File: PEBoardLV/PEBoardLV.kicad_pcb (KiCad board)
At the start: 2 copper layers, 113.7 x 78.7 mm, 69 parts, among them J1 BSPD Test Jumper, J10 ECU Debug Connector, J11 SWD Header, J12 Extra Pin Header, J13 CAN Header, J14 UART Header, J15 To TSAL, J2 Beam Interlock, J3 To HV Interlocks, J4 To Left Panel, J5 To Right Panel, J6 To Brake Light, J7 To PE HV, J8 BSPD Reset, J9 Main LV Connector, U1 MCP6004, U10 ISO1050, U11 STM32F405, U2 4072, U3 4071, U4 DE1A1B-L2-12V, U5 74HC595, U6 LM555N, U7 SN754410, U8 NCP1117DT33RKG, U9 L78S05CV-DG, Y1 8MHz

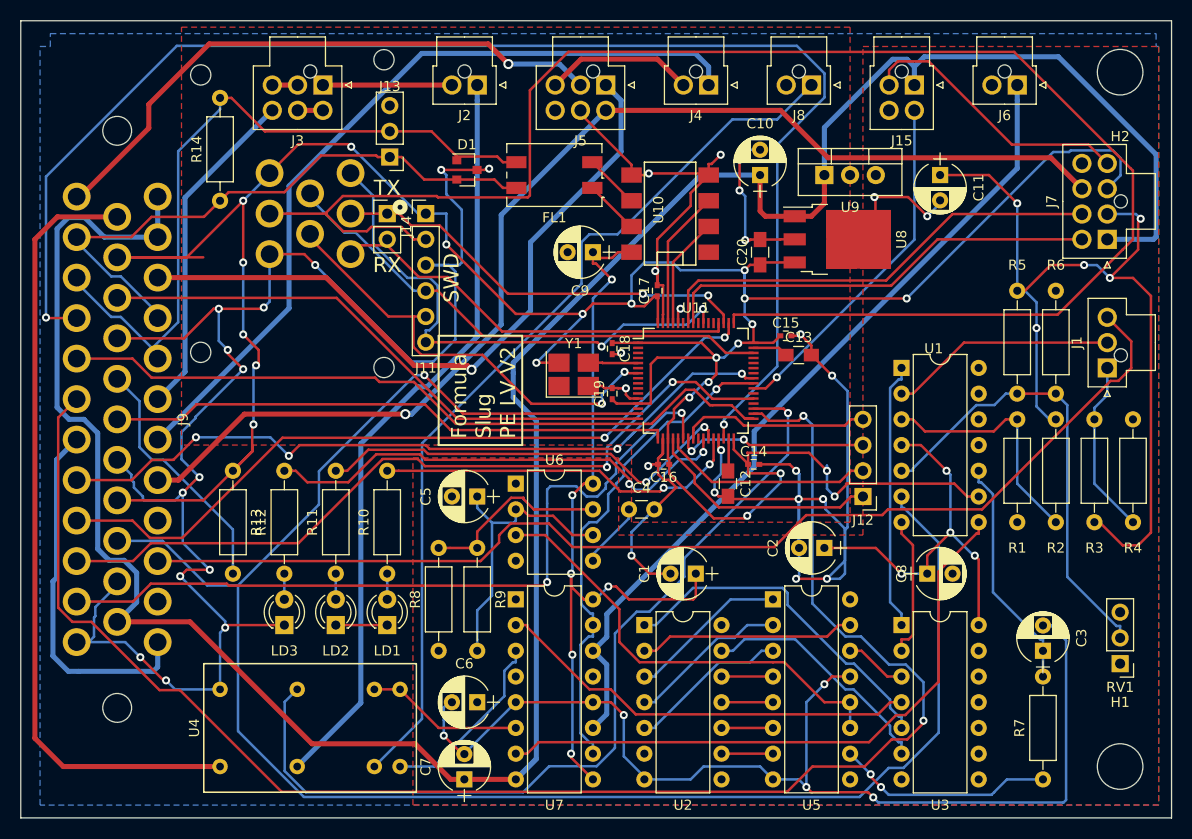
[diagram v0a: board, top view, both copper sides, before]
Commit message: Add more ground/vcc plane bridges to PE LV pcb
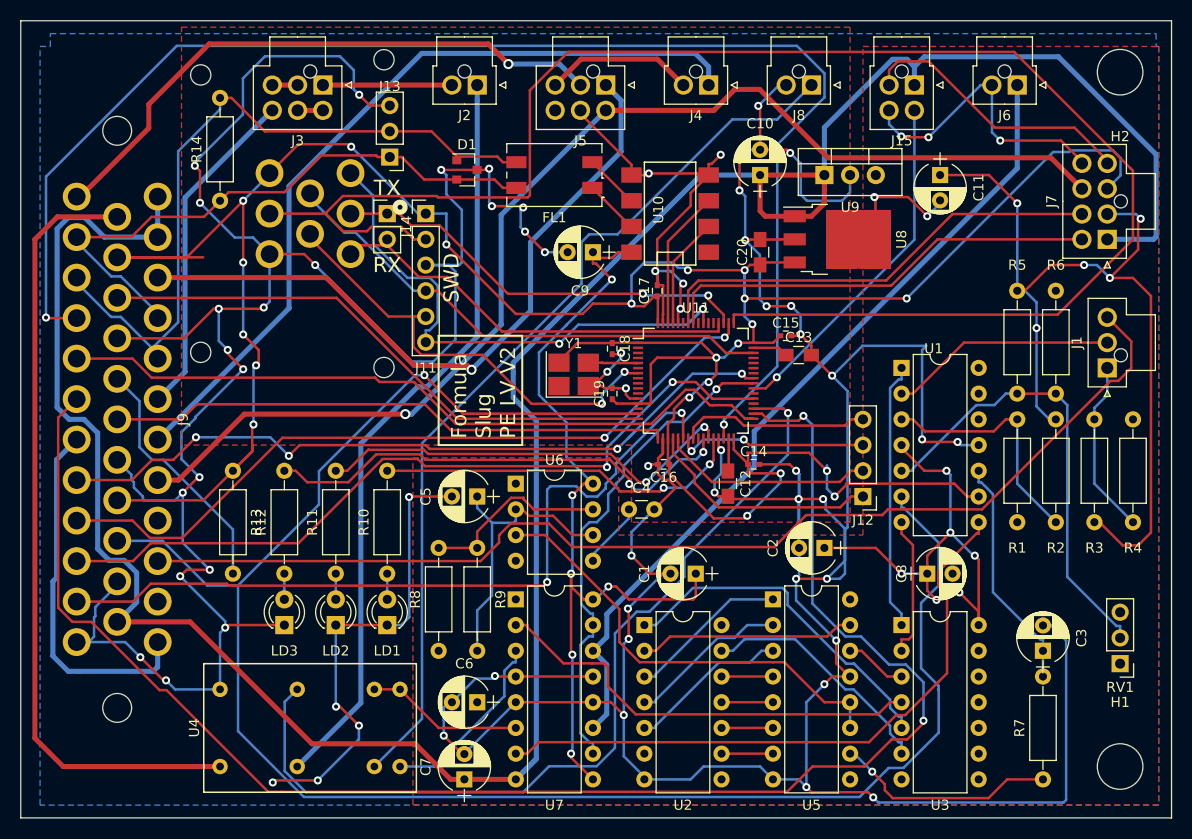
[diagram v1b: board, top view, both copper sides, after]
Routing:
- net GND: track 460.5 -> 703.4 mm, vias 41 -> 68
- net +5V: track 226.0 -> 240.6 mm, vias 17 -> 18
- net +12V: track 256.8 -> 263.1 mm
- net +3V3: track 307.8 -> 305.0 mm, vias 22 -> 21
- net /SWO: track 52.8 -> 54.7 mm
- net /AIRS_FINAL: track 116.0 -> 117.7 mm
- net /SIG_BSE: track 179.3 -> 180.7 mm
- net /BSPD_FLT: track 42.4 -> 43.5 mm
- net /TIMER: track 62.2 -> 62.9 mm

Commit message: Select 4 layer version of PE LV board
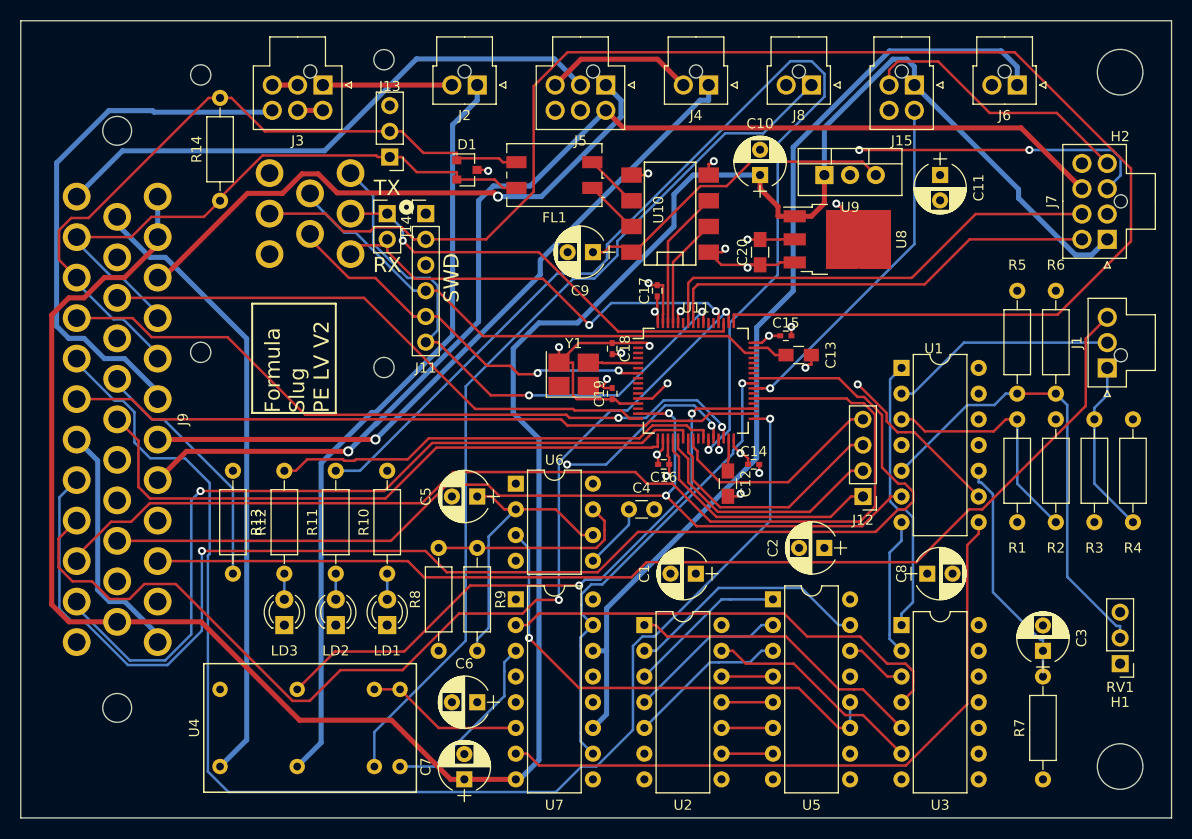
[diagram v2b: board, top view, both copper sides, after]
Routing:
- net GND: track 703.4 -> 50.7 mm, vias 68 -> 16
- net +3V3: track 305.0 -> 108.5 mm, vias 21 -> 11
- net +5V: track 240.6 -> 51.2 mm, vias 18 -> 0
- net /BUTTON_3: track 159.7 -> 68.4 mm, vias 2 -> 0
- net /SIG_BSE: track 180.7 -> 94.6 mm, vias 1 -> 2
- net /BUTTON_1: track 140.5 -> 70.9 mm
- net /STATUS_LED_2: track 42.2 -> 109.5 mm, vias 2 -> 1
- net /LED_AMS: track 74.4 -> 137.5 mm, vias 4 -> 1
- net /BUTTON_2: track 72.9 -> 132.9 mm, vias 0 -> 1
- net /LED_BSPD: track 76.7 -> 107.2 mm, vias 2 -> 0
- net /LED_IMD: track 74.5 -> 103.1 mm
- net /BSPD_FLT_LATCHED: track 88.4 -> 60.9 mm, vias 1 -> 2
- net +12V: track 263.1 -> 236.1 mm
- net /AIRS_PEINTERLOCKS_OUT: track 33.2 -> 53.1 mm
- net /AIRS_BOTS_OUT: track 77.8 -> 61.6 mm
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- added copper zone on In1.Cu, net +3V3
- added copper zone on In1.Cu, net +5V
- added copper zone on In2.Cu, net GND
- removed copper zone on F.Cu, net +3V3
- removed copper zone on F.Cu, net +5V
- removed copper zone on B.Cu, net GND
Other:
- copper layers 2 -> 4

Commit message: Revise boards based on design review
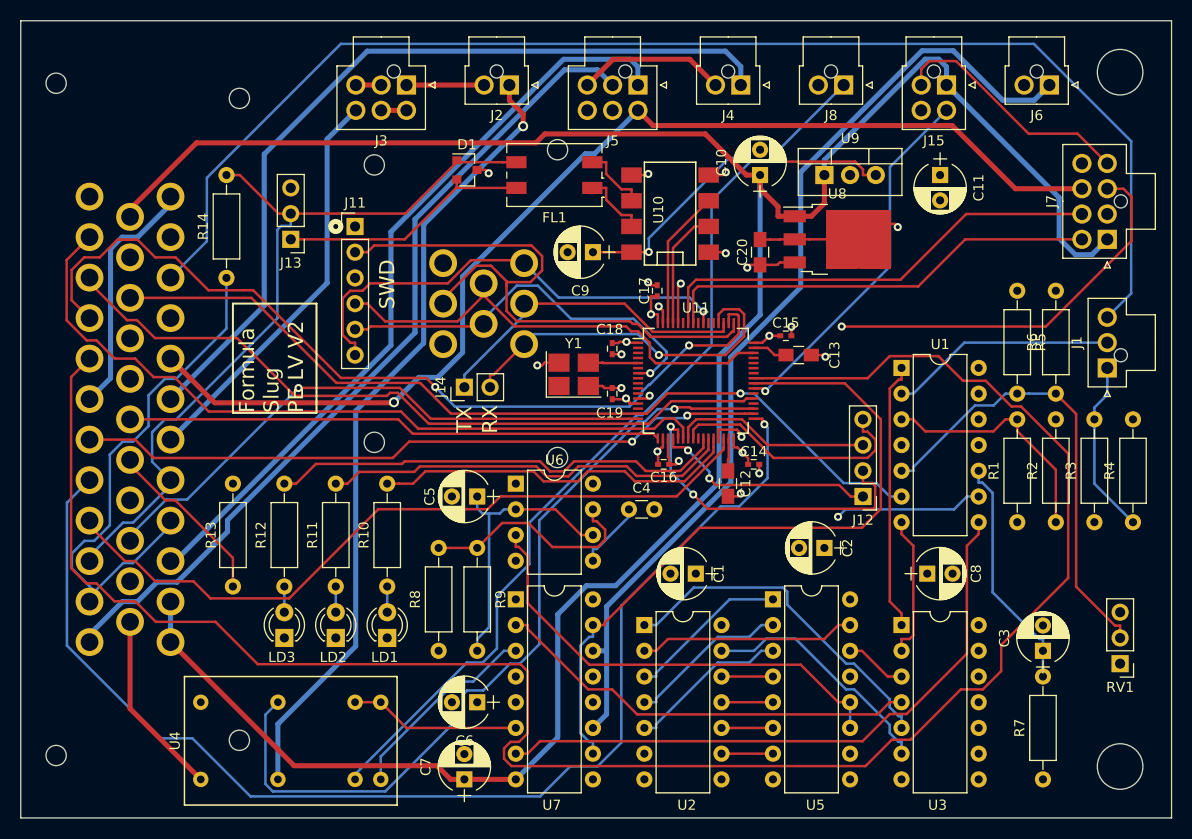
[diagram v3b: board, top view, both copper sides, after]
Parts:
- J9: footprint FSFootprints:Ampseal - 35 pin -> FSFootprints:Ampseal-776231; moved to B.Cu
- moved J10 19.3 mm to (97.2, 57.1)
- moved J14 18.8 mm to (95.2, 65.4), turned to 90 degrees
- moved J13 12.7 mm to (78.1, 50.8)
- moved J3 8.25 mm to (89.5, 35.6)
- moved R14 7.65 mm to (71.8, 54.6)
- moved J11 7.10 mm to (84.5, 49.5)
- moved J15 3.18 mm to (142.9, 35.6)
- moved J4 3.18 mm to (122.6, 35.6)
- moved J8 3.18 mm to (132.7, 35.6)
- moved J2 3.17 mm to (99.7, 35.6)
- moved J5 3.17 mm to (112.4, 35.6)
- moved J6 3.17 mm to (153.0, 35.6)
- moved U4 2.29 mm to (76.8, 96.5)
- moved R10 1.27 mm to (87.6, 85.1)
- moved R11 1.27 mm to (82.5, 85.1)
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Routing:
- net /SWCLK: track 155.2 -> 60.8 mm
- net /STATUS_LED_2: track 109.5 -> 40.9 mm, vias 1 -> 0
- net /LED_AMS: track 137.5 -> 194.4 mm, vias 1 -> 0
- net /AIRS_BOTS_OUT: track 61.6 -> 18.5 mm
- net /LED_BSPD: track 107.2 -> 73.1 mm
- net /12V_LVMS: track 56.5 -> 83.4 mm
- net +3V3: track 108.5 -> 82.3 mm
- net /CAN_H: track 60.6 -> 85.0 mm
- net /SIG_BRAKELT: track 46.4 -> 70.4 mm, vias 1 -> 0
- net /SIG_CURRENT: track 109.0 -> 130.5 mm
- net /BSPD_FLT_LATCHED: track 60.9 -> 81.1 mm, vias 2 -> 1
- net +5V: track 51.2 -> 33.6 mm, vias 0 -> 2
- net /12V_SRC: track 58.0 -> 75.4 mm, vias 1 -> 0
- net /LED_IMD: track 103.1 -> 86.3 mm
- net /AIRS_PEINTERLOCKS_OUT: track 53.1 -> 40.1 mm
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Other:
- net class 3.3V: clearance 0.205 -> 0.24
- net class Default: clearance 0.205 -> 0.24
- net class Ground: clearance 0.205 -> 0.24
- net class HighSpeed: clearance 0.205 -> 0.24
- rule trace_clearance: 0.205 -> 0.24

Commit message: Add connections to connectors on PE and Acc LV boards
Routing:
- net +5V: track 33.6 -> 54.6 mm
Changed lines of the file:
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@@
   (general
     (links 232)
-    (no_connects 1)
+    (no_connects 0)
     (area 45.804999 27.715 165.150001 109.545)
     (thickness 1.6)
     (drawings 13)
-    (tracks 940)
+    (tracks 946)
     (zones 0)
     (modules 69)
@@
   (layers
     (0 F.Cu signal)
-    (1 In1.Cu power hide)
-    (2 In2.Cu power hide)
+    (1 In1.Cu power)
+    (2 In2.Cu power)
     (31 B.Cu signal)
     (32 B.Adhes user)
@@
     (effects (font (size 1.5 1.5) (thickness 0.3)))
   )
+  (segment (start 158.75 48.3) (end 159.552 48.3) (width 0.25) (layer In1.Cu) (net 1) (status C00000))
+  (segment (start 159.552 48.3) (end 161.925 50.673) (width 0.25) (layer In1.Cu) (net 1) (status 400000))
+  (segment (start 161.925 50.673) (end 161.925 54.102) (width 0.25) (layer In1.Cu) (net 1))
+  (segment (start 161.925 54.102) (end 161.163 53.34) (width 0.25) (layer In1.Cu) (net 1))
+  (segment (start 161.163 53.34) (end 152.4 53.34) (width 0.25) (layer In1.Cu) (net 1))
+  (segment (start 152.4 53.34) (end 149.86 55.88) (width 0.25) (layer In1.Cu) (net 1) (status 800000))
   (via (at 122.7642 42.7522) (size 0.8) (layers F.Cu B.Cu) (net 1))
   (via (at 113.4667 52.05) (size 0.8) (layers F.Cu B.Cu) (net 1))

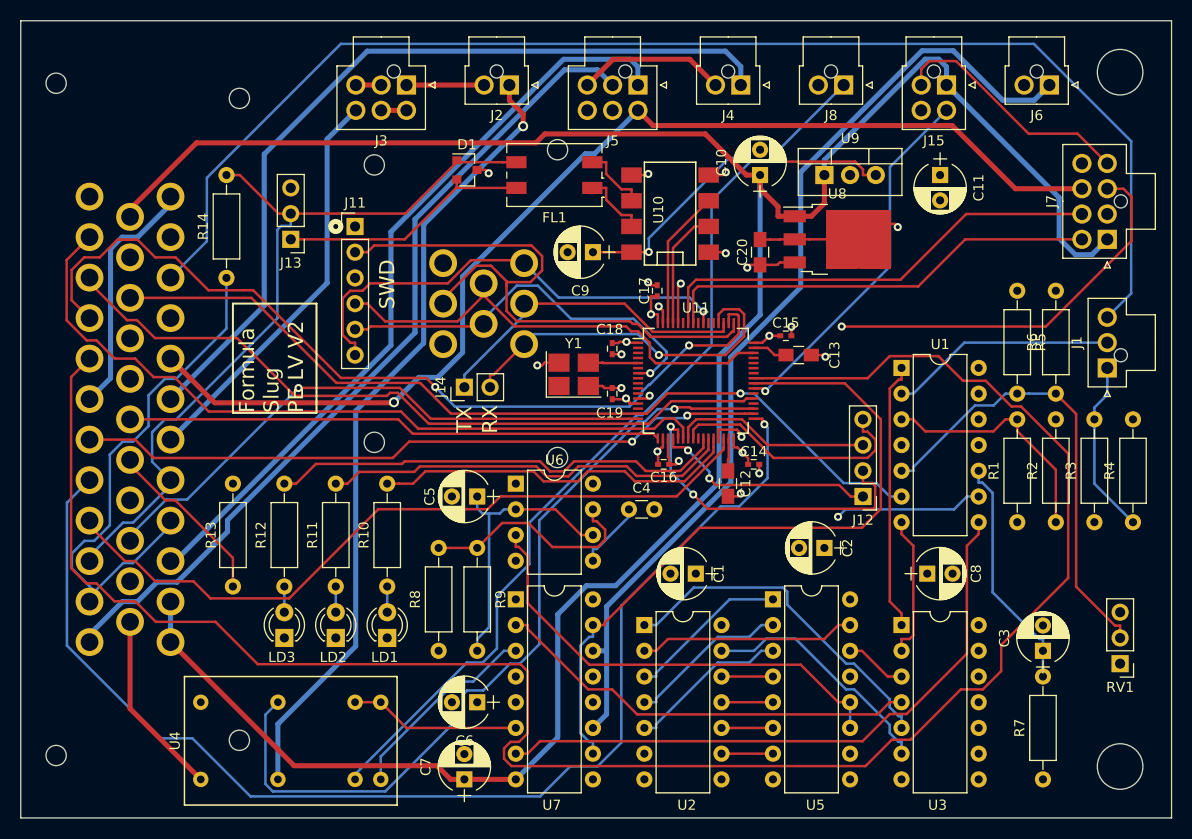
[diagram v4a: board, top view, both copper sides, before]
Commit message: Reverse connector directions on PE LV board
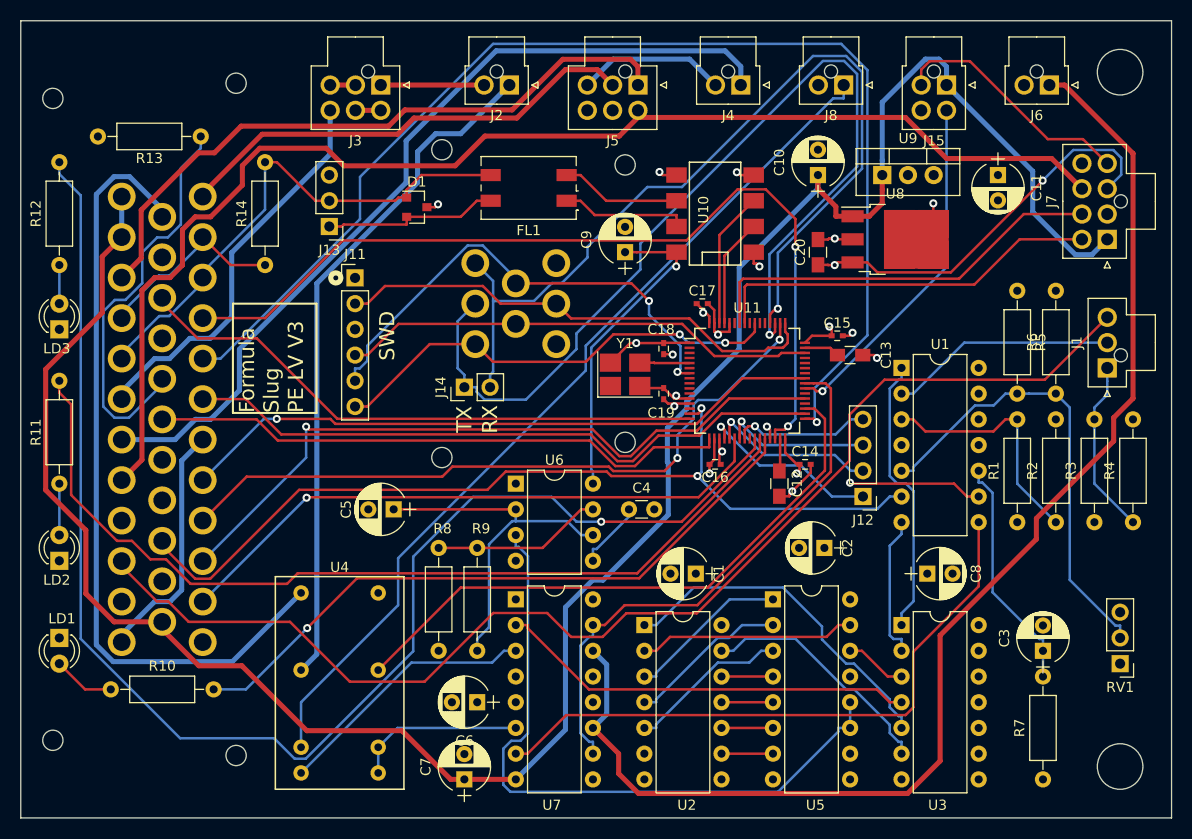
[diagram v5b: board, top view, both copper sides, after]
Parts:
- moved R12 38.8 mm to (55.2, 53.3)
- moved LD3 37.7 mm to (55.2, 59.7)
- moved R13 36.8 mm to (59.1, 40.6), turned to 0 degrees
- moved LD1 32.4 mm to (55.2, 90.2), turned to 270 degrees
- moved R11 29.1 mm to (55.2, 74.9)
- moved R10 29.1 mm to (60.3, 95.2), turned to 0 degrees
- moved LD2 28.3 mm to (55.2, 82.5)
- moved U4 10.4 mm to (86.7, 93.3), turned to 180 degrees
- moved C5 8.35 mm to (88.3, 77.5)
- moved D1 6.17 mm to (90.6, 47.6)
- moved C10 5.72 mm to (130.2, 44.5)
- moved C20 5.72 mm to (130.2, 52.1)
- moved C11 5.72 mm to (148.0, 44.5)
- moved U9 5.72 mm to (136.5, 44.5)
- moved U8 5.71 mm to (137.8, 50.8)
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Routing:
- net /LED_AMS: track 194.4 -> 64.1 mm, vias 0 -> 1
- net /STATUS_LED_3: track 45.4 -> 140.6 mm, vias 0 -> 1
- net /UART_TX: track 32.4 -> 96.5 mm, vias 0 -> 1
- net /AIRS_BOTS_OUT: track 18.5 -> 77.5 mm
- net /UART_RX: track 35.6 -> 89.5 mm
- net /STATUS_LED_2: track 40.9 -> 90.1 mm
- net /CAN_H: track 85.0 -> 44.6 mm
- net /12V_LVMS: track 83.4 -> 46.5 mm
- net /BRAKELT_H: track 96.9 -> 127.2 mm
- net /STATUS_LED_1: track 36.5 -> 65.5 mm, vias 0 -> 1
- net /CAN_L: track 78.4 -> 51.2 mm
- net Net-(J9-Pad17): track 17.3 -> 40.1 mm
- net /BSPD_FLT_LATCHED: track 81.1 -> 59.8 mm, vias 1 -> 0
- net /CLK: track 45.8 -> 66.8 mm
- net +12V: track 241.1 -> 223.1 mm
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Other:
- board text added: "Formula Slug PE LV V3"
- board text removed: "Formula Slug PE LV V2"

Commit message: edit PCBs based on actual parts that have arrived
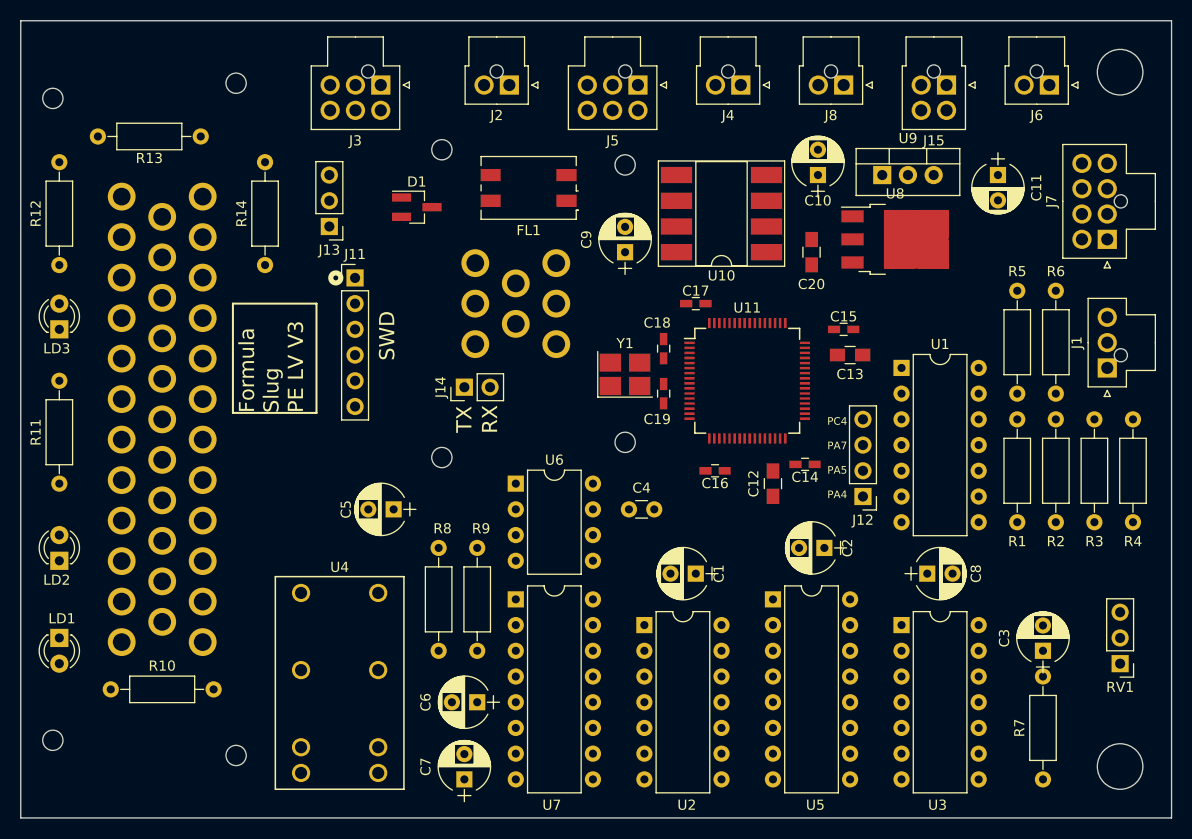
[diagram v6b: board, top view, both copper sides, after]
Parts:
- C14, C15, C16, C17, C18, C19: footprint Capacitors_SMD:C_0402 -> Capacitors_SMD:C_0603_HandSoldering
- D1: footprint TO_SOT_Packages_SMD:SOT-23 -> TO_SOT_Packages_SMD:SOT-23_Handsoldering
- U10: footprint SMD_Packages:DIP-8_SMD -> Housings_DIP:DIP-8_W8.89mm_SMDSocket_LongPads
- moved C15 0.90 mm to (132.7, 59.7)
- moved C20 0.64 mm to (129.5, 52.1)
- moved C17 0.64 mm to (118.1, 57.1)
- moved U10 0.64 mm to (120.7, 48.3), turned to 180 degrees
- moved C12 0.63 mm to (125.7, 74.9)
- moved C16 0.63 mm to (120.0, 73.7)
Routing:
- net +12V: track 223.1 -> 0.00 mm
- net /STATUS_LED_3: track 140.6 -> 0.00 mm, vias 1 -> 0
- net /AIRS_FINAL: track 127.7 -> 0.00 mm
- net /BRAKELT_H: track 127.2 -> 0.00 mm
- net /SIG_CURRENT: track 122.1 -> 0.00 mm
- net /BUTTON_2: track 120.4 -> 0.00 mm, vias 1 -> 0
- net /UART_TX: track 96.5 -> 0.00 mm, vias 1 -> 0
- net /STATUS_LED_2: track 90.1 -> 0.00 mm
- net /SIG_BSE: track 89.7 -> 0.00 mm, vias 2 -> 0
- net /UART_RX: track 89.5 -> 0.00 mm, vias 1 -> 0
- net /BSPD_RESET: track 88.2 -> 0.00 mm
- net /BUTTON_1: track 88.1 -> 0.00 mm, vias 2 -> 0
- net +3V3: track 85.5 -> 0.00 mm, vias 10 -> 0
- net /AIRS_ACC_OUT: track 84.3 -> 0.00 mm
- net /AIRS_BOTS_OUT: track 77.5 -> 0.00 mm
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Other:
- board text added: "PC4 PA7 PA5 PA4"
